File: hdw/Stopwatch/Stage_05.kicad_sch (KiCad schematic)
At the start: 5 parts, among them U1301 4026, U1302 HDSP-7503

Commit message: started sch work
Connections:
- net Count_Reset: no longer names the net of U1301.15 (Reset)
- net Stage04_Clock_Out: no longer names the net of R1301.1, U1301.1 (Clock)
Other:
- moved on the sheet: C1301

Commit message: adjusted stage sheet
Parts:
- removed C1301: 0.1uF, Capacitors_SMD:C_0603, symbol Custom_Library:C_Custom
- removed R1301: 10k, Resistors_SMD:R_0603, symbol Custom_Library:R_Custom
- removed RN1301: 1k, Resistor_SMD:R_Cat16-8, symbol Device:R_Pack08
- removed U1301: 4026, Housings_SSOP:TSSOP-16_4.4x5mm_Pitch0.65mm, symbol Custom_Library:4026
- removed U1302: HDSP-7503, Display_7Segment:HDSP-A151, symbol Display_Character:HDSP-7503
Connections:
- no-connect marks 5 -> 0

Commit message: added some more junk
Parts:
- added C?: 0.1uF, Capacitors_SMD:C_0603, symbol Custom_Library:C_Custom
- added R?: 10k, Resistors_SMD:R_0603, symbol Custom_Library:R_Custom
- added RN?: 1k, Resistor_SMD:R_Cat16-8, symbol Device:R_Pack08
- added U?: 4026, Housings_SSOP:TSSOP-16_4.4x5mm_Pitch0.65mm, symbol Custom_Library:4026
- added U?: HDSP-7503, Display_7Segment:HDSP-A151, symbol Display_Character:HDSP-7503
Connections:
- new net: RN?.10 (R7.2), U?.3 (G)
- new net: RN?.11 (R6.2), U?.2 (F)
- new net: RN?.12 (R5.2), U?.4 (E)
- new net: RN?.13 (R4.2), U?.5 (D)
- new net: RN?.14 (R3.2), U?.8 (C)
- new net: RN?.15 (R2.2), U?.9 (B)
- new net: RN?.16 (R1.2), U?.10 (A)
- new net +3V3: C?.1, U?.16 (VDD)
- new net Count_Reset: U?.15 (Reset)
- new net Display_Enable: U?.3 (Display_Enable_In)
- new net GND: C?.2, R?.2, U?.1 (CC), U?.2 (Clock_Inhibit), U?.6 (CC), U?.8 (VSS)
- new net Minutes_Reset: R?.1, U?.1 (Clock)
- new net Stage05_Clock_Out: U?.5 (Carry_Out)
- new net Stage05_SEG_A: RN?.1 (R1.1), U?.10 (a)
- new net Stage05_SEG_B: RN?.2 (R2.1), U?.12 (b)
- new net Stage05_SEG_C: RN?.3 (R3.1), U?.13 (c)
- new net Stage05_SEG_D: RN?.4 (R4.1), U?.9 (d)
- new net Stage05_SEG_E: RN?.5 (R5.1), U?.11 (e)
- new net Stage05_SEG_F: RN?.6 (R6.1), U?.6 (f)
- new net Stage05_SEG_G: RN?.7 (R7.1), U?.7 (g)
- no-connect marks 0 -> 5

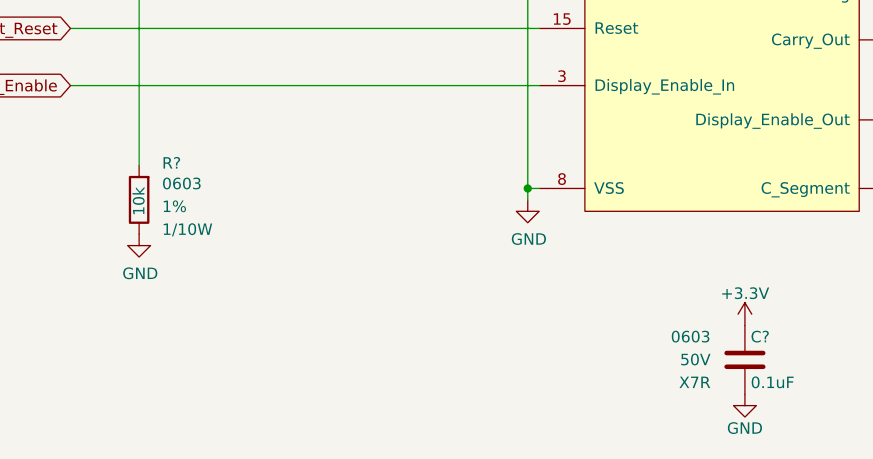
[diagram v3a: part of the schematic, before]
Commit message: Assigned some digikey pns
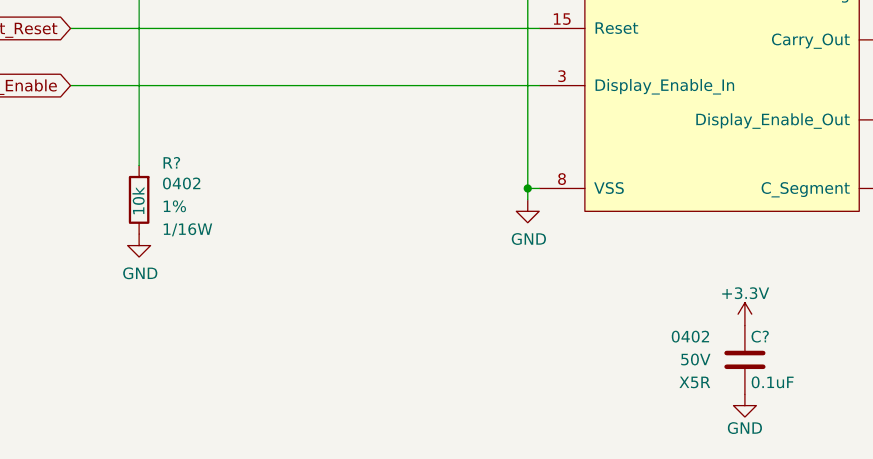
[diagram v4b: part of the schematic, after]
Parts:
- C?: footprint Capacitors_SMD:C_0603 -> Capacitors_SMD:C_0402; Dielectric X7R -> X5R; Digi-Key PN 311-1344-1-ND -> 490-10697-1-ND; display_footprint 0603 -> 0402
- R?: footprint Resistors_SMD:R_0603 -> Resistors_SMD:R_0402; Digi-Key PN RMCF0603FT10K0CT-ND -> RMCF0402FT10K0CT-ND; Wattage 1/10W -> 1/16W; display_footprint 0603 -> 0402
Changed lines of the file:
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@@
       (effects (font (size 1.27 1.27)) (justify left))
     )
-    (property "Footprint" "Resistors_SMD:R_0603" (at 63.5 111.76 0)
+    (property "Footprint" "Resistors_SMD:R_0402" (at 63.5 111.76 0)
       (effects (font (size 1.27 1.27)) hide)
     )
@@
       (effects (font (size 1.27 1.27)) hide)
     )
-    (property "display_footprint" "0603" (at 66.04 109.982 0)
+    (property "display_footprint" "0402" (at 66.04 109.982 0)
       (effects (font (size 1.27 1.27)) (justify left))
     )
@@
       (effects (font (size 1.27 1.27)) (justify left))
     )
-    (property "Wattage" "1/10W" (at 66.04 115.062 0)
+    (property "Wattage" "1/16W" (at 66.04 115.062 0)
       (effects (font (size 1.27 1.27)) (justify left))
     )
-    (property "Digi-Key PN" "RMCF0603FT10K0CT-ND" (at 71.12 101.6 0)
+    (property "Digi-Key PN" "RMCF0402FT10K0CT-ND" (at 71.12 101.6 0)
       (effects (font (size 1.524 1.524)) hide)
     )
@@
       (effects (font (size 1.27 1.27)) (justify left))
     )
-    (property "Footprint" "Capacitors_SMD:C_0603" (at 131.7752 133.35 0)
+    (property "Footprint" "Capacitors_SMD:C_0402" (at 131.7752 133.35 0)
       (effects (font (size 1.27 1.27)) hide)
     )
@@
       (effects (font (size 1.27 1.27)) hide)
     )
-    (property "display_footprint" "0603" (at 127 127 0)
+    (property "display_footprint" "0402" (at 127 127 0)
       (effects (font (size 1.27 1.27)) (justify right))
     )
@@
       (effects (font (size 1.27 1.27)) (justify right))
     )
-    (property "Dielectric" "X7R" (at 127 132.08 0)
+    (property "Dielectric" "X5R" (at 127 132.08 0)
       (effects (font (size 1.27 1.27)) (justify right))
     )
-    (property "Digi-Key PN" "311-1344-1-ND" (at 141.605 116.84 0)
+    (property "Digi-Key PN" "490-10697-1-ND" (at 141.605 116.84 0)
       (effects (font (size 1.524 1.524)) hide)
     )

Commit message: lots and lots of routing
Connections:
- net +3V3 renamed +3.3V
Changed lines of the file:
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@@
     )
   )
-  (symbol (lib_id "Incrementor-rescue:+3.3V-power") (at 106.68 68.58 0) (unit 1)
+  (symbol (lib_id "power:+3.3V") (at 106.68 68.58 0) (unit 1)
     (in_bom yes) (on_board yes) (dnp no)
     (property "Reference" "#PWR?" (at 106.68 72.39 0)
@@
     )
   )
-  (symbol (lib_id "Incrementor-rescue:+3.3V-power") (at 130.81 125.73 0) (unit 1)
+  (symbol (lib_id "power:+3.3V") (at 130.81 125.73 0) (unit 1)
     (in_bom yes) (on_board yes) (dnp no)
     (property "Reference" "#PWR?" (at 130.81 129.54 0)
